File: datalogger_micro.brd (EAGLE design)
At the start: 32 x 40.6 mm, 47 parts, among them IC1 DS3231/SO, IC2 LD117AS33TR, M1 PAT, M2 PAT, Q2 IRLML5203

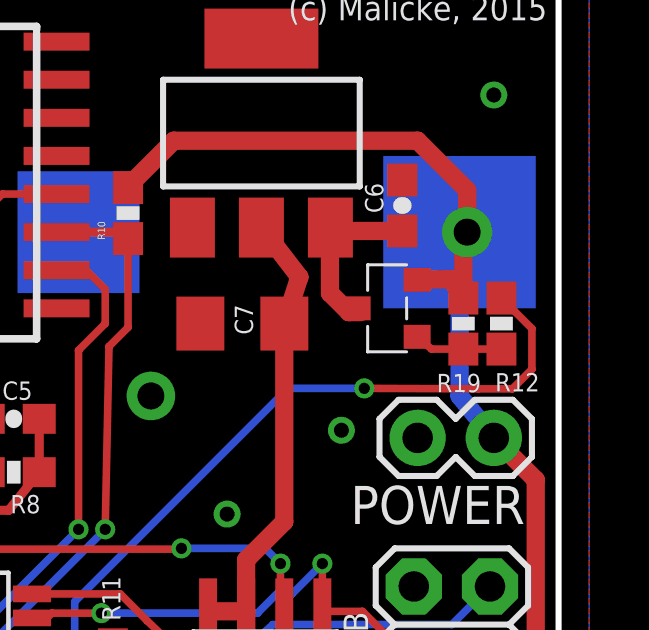
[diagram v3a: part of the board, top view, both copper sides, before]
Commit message: VCC-ST active low
VCC ST is now active low by p channel mosfet
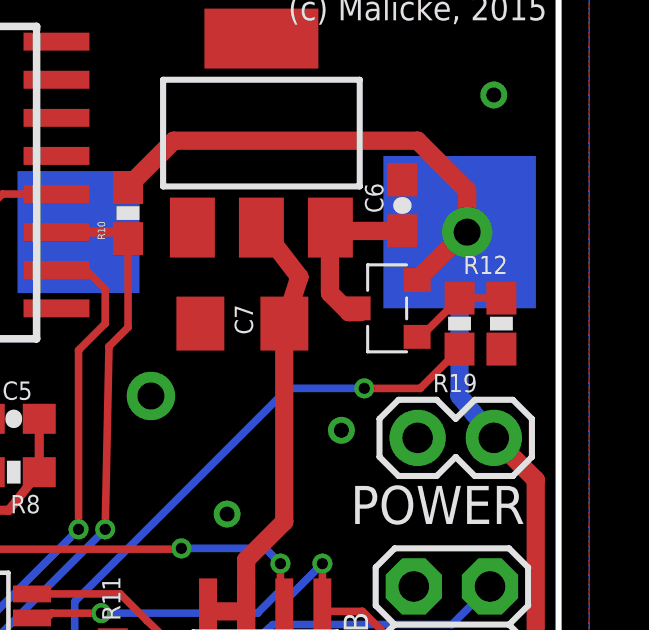
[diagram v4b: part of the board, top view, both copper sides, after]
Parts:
- R12: value 100k -> 10k
- R19: value 100k -> 1k
- moved R19 0.13 mm to (33.7, 31.2)
- turned R12 to 270 degrees
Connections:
- net GND: now also R12.2
- net N$11: now also R19.1; no longer R19.2
- net VBAT: no longer R19.1
- net VCC/ST_ON: now also R19.2; no longer R12.2
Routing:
- net VCC/ST_ON: track 24.8 -> 19.9 mm
- net VBAT: track 132.6 -> 130.8 mm
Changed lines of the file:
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@@
 <attribute name="VALUE" x="16.383" y="16.4084" size="0.8128" layer="27" rot="R90"/>
 </element>
-<element name="R12" library="SparkFun" package="0603-RES" value="100k" x="35.052" y="31.242" smashed="yes" rot="R90">
-<attribute name="NAME" x="36.322" y="29.591" size="0.6096" layer="25" font="vector" rot="R180"/>
-<attribute name="VALUE" x="36.195" y="30.226" size="0.4064" layer="27" font="vector" rot="R90"/>
+<element name="R12" library="SparkFun" package="0603-RES" value="10k" x="35.052" y="31.242" smashed="yes" rot="R270">
+<attribute name="NAME" x="33.782" y="32.893" size="0.6096" layer="25" font="vector"/>
+<attribute name="VALUE" x="33.909" y="32.258" size="0.4064" layer="27" font="vector" rot="R270"/>
 </element>
 <element name="32.768KHZ" library="crystal" package="TC38H" value="" x="20.193" y="14.732" smashed="yes" rot="R46">
@@
 <attribute name="VALUE" x="34.642" y="30.25" size="1.778" layer="27" rot="R90"/>
 </element>
-<element name="R19" library="SparkFun" package="0603-RES" value="100k" x="33.782" y="31.242" smashed="yes" rot="R270">
-<attribute name="NAME" x="32.893" y="28.956" size="0.6096" layer="25" font="vector"/>
-<attribute name="VALUE" x="32.639" y="32.258" size="0.4064" layer="27" font="vector" rot="R270"/>
+<element name="R19" library="SparkFun" package="0603-RES" value="1k" x="33.655" y="31.242" smashed="yes" rot="R270">
+<attribute name="NAME" x="32.766" y="28.956" size="0.6096" layer="25" font="vector"/>
+<attribute name="VALUE" x="32.512" y="32.258" size="0.4064" layer="27" font="vector" rot="R270"/>
 </element>
 </elements>
@@
 <via x="29.21" y="16.129" extent="1-16" drill="0.5" diameter="0.254"/>
 <contactref element="IC2" pad="1"/>
+<contactref element="R12" pad="2"/>
 </signal>
 <signal name="RESET">
@@
 <wire x1="22.098" y1="17.526" x2="25.4" y2="17.526" width="0.3048" layer="16"/>
 <wire x1="25.4" y1="17.526" x2="26.924" y2="19.05" width="0.3048" layer="16"/>
-<wire x1="15.513" y1="23.7236" x2="15.494" y2="23.7046" width="0" layer="19" extent="1-1"/>
+<wire x1="22.098" y1="17.526" x2="22.098" y2="18.835" width="0.3048" layer="1"/>
+<wire x1="15.494" y1="23.7046" x2="15.513" y2="23.7236" width="0" layer="19" extent="1-1"/>
 <wire x1="27.813" y1="13.843" x2="27.813" y2="13.91" width="0" layer="19" extent="1-1"/>
-<wire x1="22.098" y1="17.526" x2="22.098" y2="18.835" width="0.3048" layer="1"/>
 </signal>
 <signal name="VCC/ST_ON">
@@
 <wire x1="20.828" y1="19.812" x2="19.4246" y2="19.812" width="0.254" layer="1"/>
 <wire x1="19.4246" y1="19.812" x2="19.4056" y2="19.831" width="0.254" layer="1"/>
-<wire x1="30.48" y1="29.083" x2="34.274" y2="29.067" width="0.254" layer="1"/>
 <wire x1="20.828" y1="19.812" x2="20.828" y2="21.971" width="0.254" layer="16"/>
-<contactref element="R12" pad="2"/>
-<wire x1="34.274" y1="29.067" x2="35.417" y2="29.067" width="0.254" layer="1"/>
-<wire x1="35.417" y1="29.067" x2="36.068" y2="29.718" width="0.254" layer="1"/>
-<wire x1="36.068" y1="29.718" x2="36.068" y2="31.076" width="0.254" layer="1"/>
-<wire x1="36.068" y1="31.076" x2="35.052" y2="32.092" width="0.254" layer="1"/>
 <wire x1="20.828" y1="21.971" x2="27.94" y2="29.083" width="0.254" layer="16"/>
 <wire x1="27.94" y1="29.083" x2="30.48" y2="29.083" width="0.254" layer="16"/>
+<contactref element="R19" pad="2"/>
+<wire x1="30.48" y1="29.083" x2="32.346" y2="29.083" width="0.254" layer="1"/>
+<wire x1="32.346" y1="29.083" x2="33.655" y2="30.392" width="0.254" layer="1"/>
 </signal>
 <signal name="RTC_INT">
@@
 <wire x1="18.63" y1="25.019" x2="19.646" y2="26.289" width="0.3048" layer="1"/>
 <wire x1="8.763" y1="29.552" x2="8.763" y2="31.154" width="0.3048" layer="1"/>
-<contactref element="Q2" pad="2"/>
-<contactref element="R19" pad="1"/>
 <via x="33.909" y="34.29" extent="1-16" drill="0.9" diameter="1.6764"/>
 <wire x1="22.606" y1="35.775" x2="22.606" y2="35.814" width="0.6096" layer="1"/>
@@
 <wire x1="32.258" y1="37.338" x2="33.909" y2="35.687" width="0.6096" layer="1"/>
 <wire x1="33.909" y1="35.687" x2="33.909" y2="34.29" width="0.6096" layer="1"/>
-<wire x1="33.782" y1="32.092" x2="33.782" y2="34.163" width="0.6096" layer="1"/>
 <wire x1="33.782" y1="34.163" x2="33.909" y2="34.29" width="0.6096" layer="1"/>
-<wire x1="33.782" y1="32.092" x2="33.358" y2="32.727" width="0.6096" layer="1"/>
-<wire x1="33.358" y1="32.727" x2="32.242" y2="32.7" width="0.6096" layer="1"/>
-<wire x1="33.655" y1="34.29" x2="33.782" y2="34.163" width="0" layer="19" extent="1-16"/>
+<contactref element="Q2" pad="2"/>
+<wire x1="33.782" y1="34.163" x2="33.705" y2="34.163" width="0.6096" layer="1"/>
+<wire x1="33.705" y1="34.163" x2="32.242" y2="32.7" width="0.6096" layer="1"/>
+<wire x1="33.655" y1="34.29" x2="33.705" y2="34.163" width="0" layer="19" extent="1-16"/>
 <wire x1="12.9404" y1="9.5504" x2="12.827" y2="9.525" width="0" layer="19" extent="1-16"/>
 <wire x1="14.713" y1="15.1384" x2="14.732" y2="15.1194" width="0" layer="19" extent="1-1"/>
@@
 </signal>
 <signal name="N$11">
-<contactref element="R19" pad="2"/>
 <contactref element="R12" pad="1"/>
 <contactref element="Q2" pad="1"/>
-<wire x1="35.052" y1="30.392" x2="33.782" y2="30.392" width="0.254" layer="1"/>
-<wire x1="33.782" y1="30.392" x2="32.723" y2="30.392" width="0.254" layer="1"/>
-<wire x1="32.723" y1="30.392" x2="32.242" y2="30.8" width="0.254" layer="1"/>
+<contactref element="R19" pad="1"/>
+<wire x1="32.242" y1="30.8" x2="32.363" y2="30.8" width="0.254" layer="1"/>
+<wire x1="32.363" y1="30.8" x2="33.655" y2="32.092" width="0.254" layer="1"/>
+<wire x1="33.655" y1="32.092" x2="35.052" y2="32.092" width="0.254" layer="1"/>
 </signal>
 </signals>
